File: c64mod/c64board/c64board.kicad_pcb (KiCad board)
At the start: 2 copper layers, 24.1 x 53.3 mm, 13 parts, among them J1 Conn_02x10_Odd_Even, U1 VIC-II, U2 MIC5504-3.3YM5, U3 LVC257, U4 LVC245, U5 LVC245

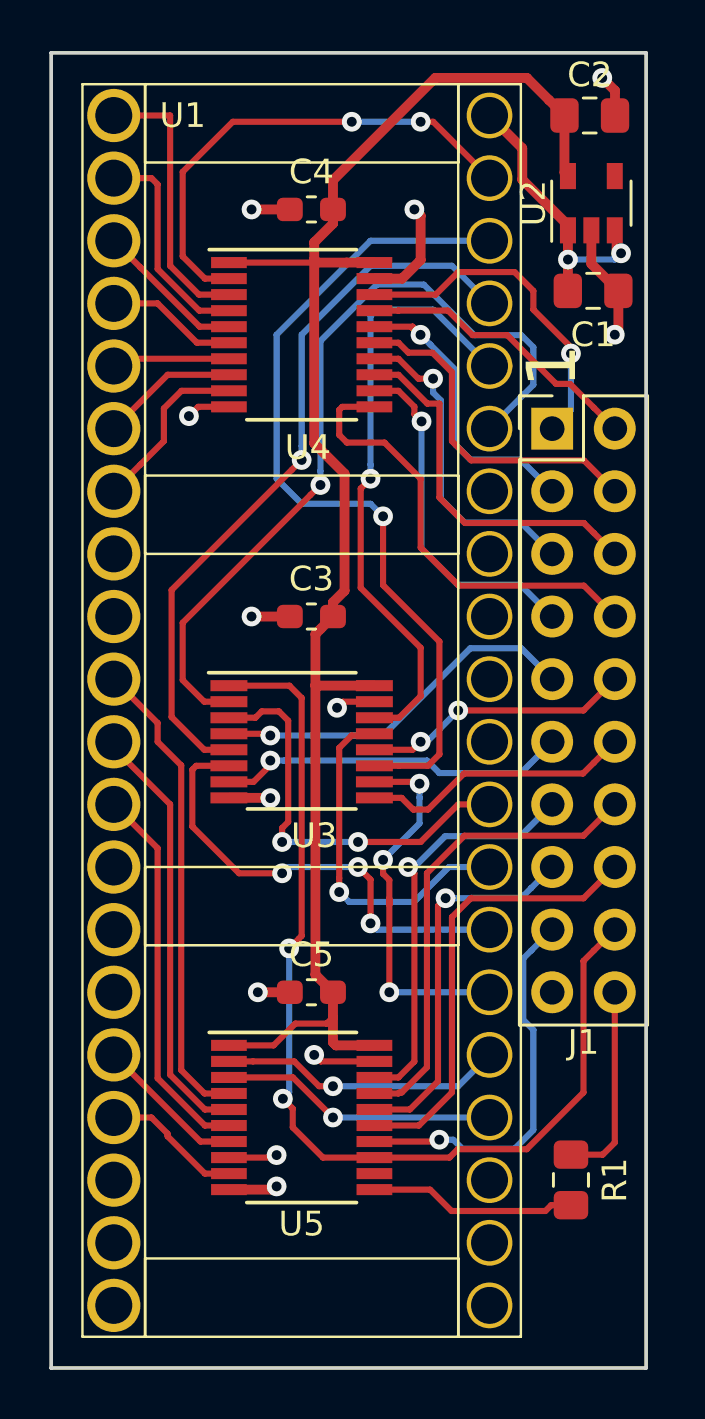
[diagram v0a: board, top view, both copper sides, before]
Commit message: Modified C64 VIC adapter for easier manufacture
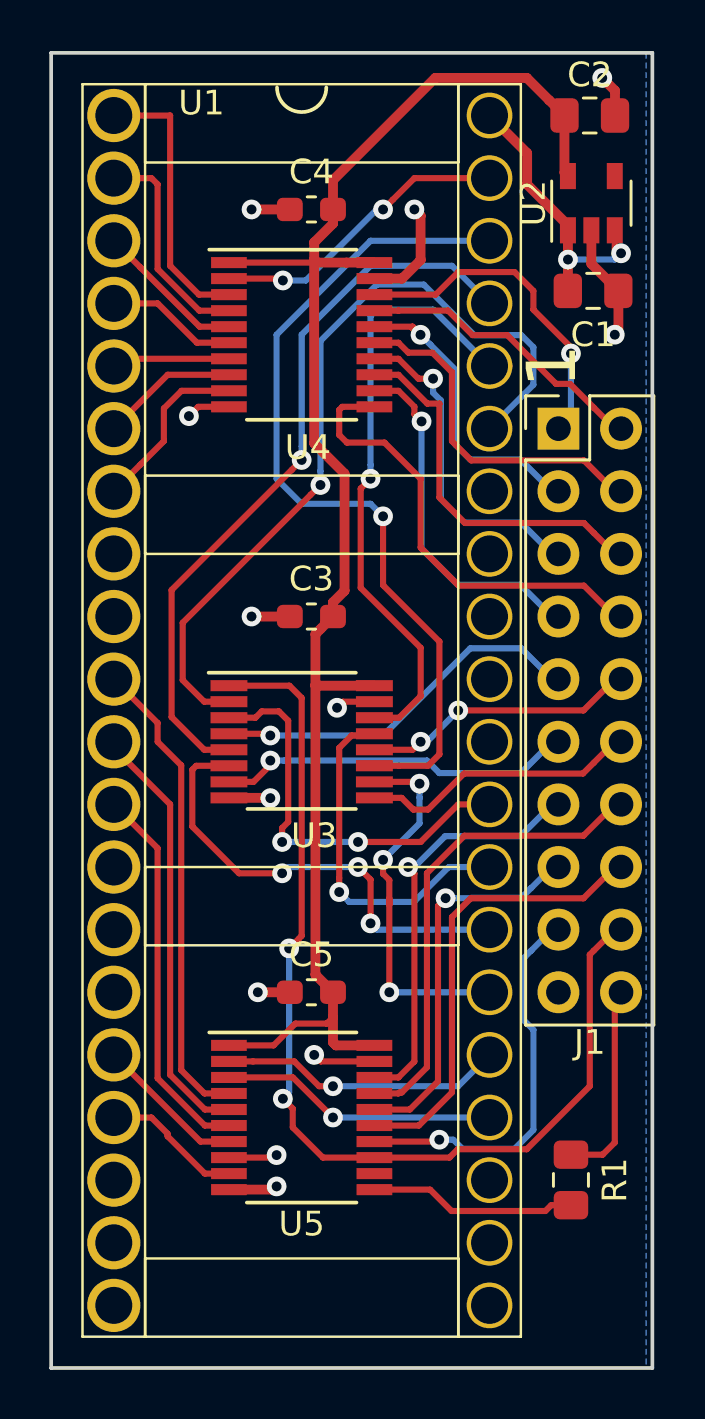
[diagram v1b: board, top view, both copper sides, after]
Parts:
- removed REF**: OSHW-Logo2_7.3x6mm_SilkScreen, Symbol:OSHW-Logo2_7.3x6mm_SilkScreen
- moved J1 0.25 mm to (152.7, 68.6)
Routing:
- net Net-(U1-Pad39): track 19.9 -> 12.3 mm
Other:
- board size 24.1 x 53.3 mm -> 24.4 x 53.3 mm
- board text added: "C64 mod Rev 3 github.com/c0pperdragon"
- board text removed: "C64 mod Rev 1 github.com/c0pperdragon"
